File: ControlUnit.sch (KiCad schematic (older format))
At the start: 30 parts, among them U601 74HCT74N, U602 74HCT08N, U603 74LS153, U604 74HCT74N, U605 74HCT244N, U606 74HCT273N, U607 74HCT273N, U608 74LS161AN, U609 74HCT244N, U610 AT28C64B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

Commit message: Libraries re-imported.  Using rescue symbols still.  Adjusted multi-byte registers to use low-byte first.. applied this convention to all multi-byte registers for consistency.
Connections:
- net ~I[10:8]->BUS is gone; now on net ~I[7:5]->RS: U616.6
- net VCC: now also U604.4 (~S); no longer U604.1 (~R)
- net ~I[7:5]->RS: no longer U616.8
- net ~RST: now also U604.1 (~R); no longer U604.4 (~S)
- net ~sext(I[10:8])->BUS: now also U616.8
- net AREG_IN renamed ALU_AREG_IN
- net TR_HALT renamed TRG_HALT
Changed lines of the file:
@@
 IR_IN
 Text HLabel 14375 5050 2    50   Output ~ 0
-AREG_IN
+ALU_AREG_IN
 Text HLabel 11275 2175 2    50   Output ~ 0
 B2
@@
 $EndComp
 Text HLabel 14325 14475 2    50   Output ~ 0
-TR_HALT
+TRG_HALT
 $Comp
 L Breadboard_CPU-rescue:74LS04-74xx U616
@@
 	1    0    0    -1
 $EndComp
-Text HLabel 4375 8050 1    50   Input ~ 0
+Text HLabel 4375 8750 3    50   Input ~ 0
 ~RST
 Wire Wire Line
-	4375 8050 4375 8100
+	4375 8750 4375 8700
 $Comp
 L Breadboard_CPU-rescue:VCC-power #PWR?
 U 1 1 6109BDDC
-P 4375 8750
+P 4375 8050
 AR Path="/5EFC0623/6109BDDC" Ref="#PWR?"  Part="1"
 AR Path="/5F05F116/6109BDDC" Ref="#PWR0604"  Part="1"
-F 0 "#PWR0604" H 4375 8600 50  0001 C CNN
-F 1 "VCC" H 4393 8923 50  0000 C CNN
-F 2 "" H 4375 8750 50  0001 C CNN
-F 3 "" H 4375 8750 50  0001 C CNN
-	1    4375 8750
-	1    0    0    1
-$EndComp
-Wire Wire Line
-	4375 8700 4375 8750
+F 0 "#PWR0604" H 4375 7900 50  0001 C CNN
+F 1 "VCC" H 4393 8223 50  0000 C CNN
+F 2 "" H 4375 8050 50  0001 C CNN
+F 3 "" H 4375 8050 50  0001 C CNN
+	1    4375 8050
+	-1   0    0    -1
+$EndComp
+Wire Wire Line
+	4375 8100 4375 8050
 Wire Wire Line
 	4025 8300 4075 8300
@@
 Wire Wire Line
 	14375 5550 13475 5550
-Text Label 16250 11725 0    50   ~ 0
-~I[10:8]->BUS
+Text Label 16250 12225 0    50   ~ 0
+~sext(I[10:8])->BUS
 Text Label 16250 11225 0    50   ~ 0
 ~I[10:8]->RS
-Text Label 16250 12225 0    50   ~ 0
+Text Label 16250 11725 0    50   ~ 0
 ~I[7:5]->RS
 Text Label 16250 12725 0    50   ~ 0

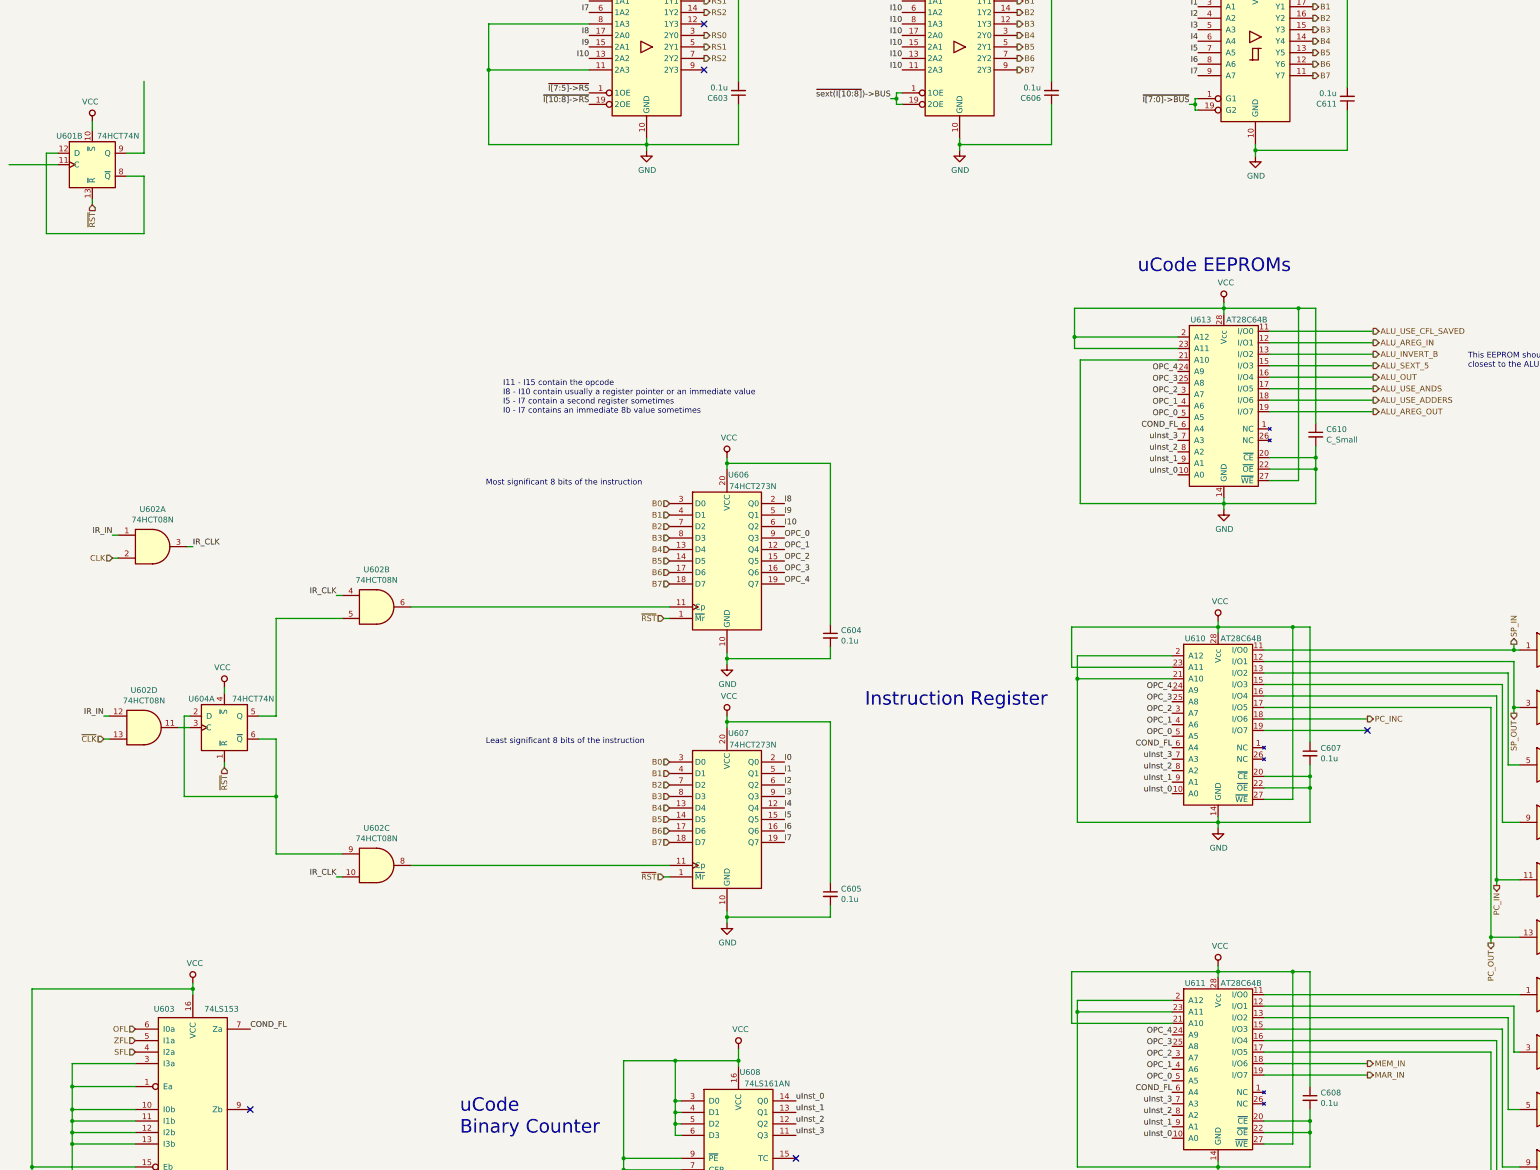
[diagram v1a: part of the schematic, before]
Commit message: Added REGS_ASSERT_RS0.  Added user referenceable CFL to solve issue of performing arithmetic on stack frame and global pointers.  TRAP routines will be created to perform ADD operations (leveraging JC/JNC) on SFP and GP.  uCode rev. 1 created in GDrive.
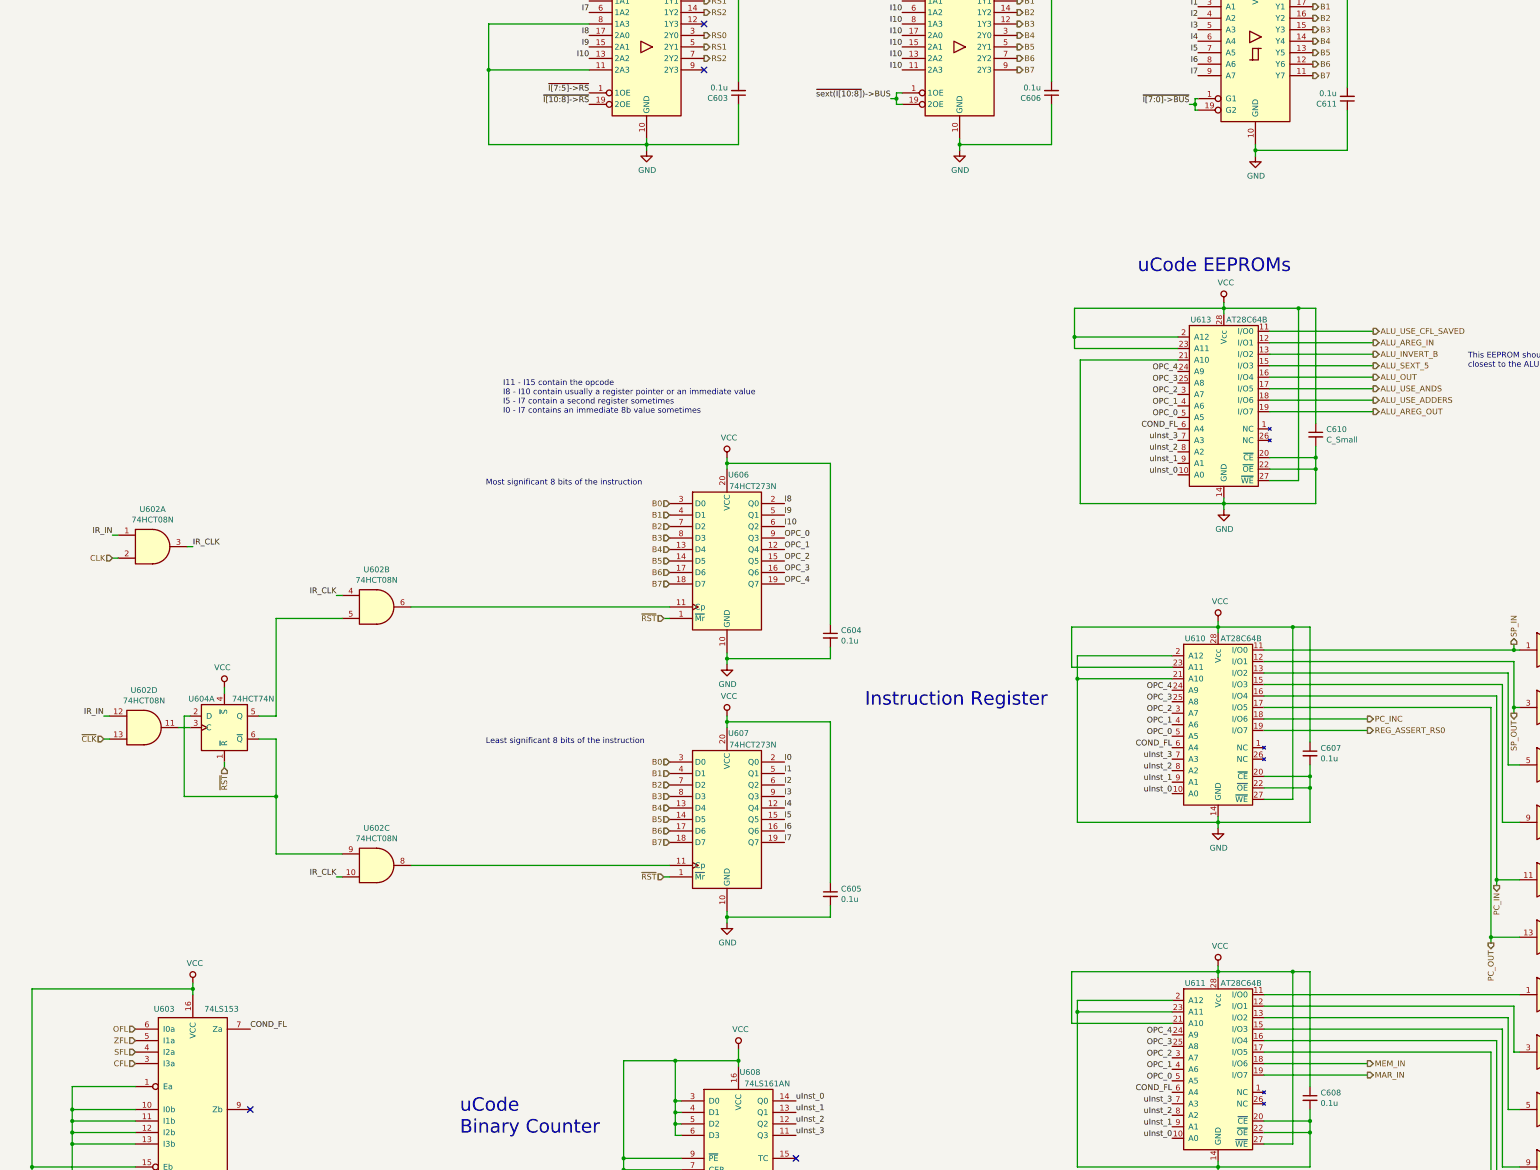
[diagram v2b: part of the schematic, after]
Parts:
- removed U601: 74HCT74N, symbol Breadboard_CPU-rescue:74LS74-74xx
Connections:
- net GND: no longer U603.3 (I3a)
- net REG_ASSERT_RS0: now reaches U610.19 (I/O7)
- new net CFL: U603.3 (I3a)
- no-connect marks 5 -> 4
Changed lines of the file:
@@
 ALU_INVERT_B
-$Comp
-L Breadboard_CPU-rescue:74LS74-74xx U601
-U 2 1 61164C73
-P 3225 3500
-AR Path="/5F05F116/61164C73" Ref="U601"  Part="2"
-AR Path="/5EFC0970/61164C73" Ref="U?"  Part="2"
-AR Path="/5EFC0623/61164C73" Ref="U?"  Part="2"
-F 0 "U601" H 3025 3750 50  0000 C CNN
-F 1 "74HCT74N" H 3450 3750 50  0000 C CNN
-F 2 "" H 3225 3500 50  0001 C CNN
-F 3 "74xx/74hc_hct74.pdf" H 3225 3500 50  0001 C CNN
-	2    3225 3500
-	1    0    0    -1
-$EndComp
-Text HLabel 3225 3850 3    50   Input ~ 0
-~RST
-Wire Wire Line
-	3225 3850 3225 3800
-$Comp
-L Breadboard_CPU-rescue:VCC-power #PWR?
-U 1 1 6119C7DB
-P 3225 3125
-AR Path="/5EFC0623/6119C7DB" Ref="#PWR?"  Part="1"
-AR Path="/5F05F116/6119C7DB" Ref="#PWR0601"  Part="1"
-F 0 "#PWR0601" H 3225 2975 50  0001 C CNN
-F 1 "VCC" H 3243 3298 50  0000 C CNN
-F 2 "" H 3225 3125 50  0001 C CNN
-F 3 "" H 3225 3125 50  0001 C CNN
-	1    3225 3125
-	-1   0    0    -1
-$EndComp
-Wire Wire Line
-	3225 3200 3225 3125
-Wire Wire Line
-	2825 3400 2925 3400
-Wire Wire Line
-	2825 4100 2825 3400
-Wire Wire Line
-	3675 4100 2825 4100
-Wire Wire Line
-	3675 3600 3675 4100
-Wire Wire Line
-	3525 3600 3675 3600
-Wire Wire Line
-	3525 3400 3675 3400
-Wire Wire Line
-	3675 3400 3675 2775
-Wire Wire Line
-	2925 3500 2500 3500
 $Comp
 L Breadboard_CPU-rescue:74LS08-74xx U?
@@
 Text HLabel 14375 4950 2    50   Output ~ 0
 ALU_USE_CFL_SAVED
-Wire Wire Line
-	3050 11525 3050 11325
-Wire Wire Line
-	3050 11325 3600 11325
-Connection ~ 3050 11525
 Text HLabel 3325 8500 0    50   Input ~ 0
 ~CLK
@@
 Text HLabel 15600 7675 1    50   Output ~ 0
 SP_IN
-NoConn ~ 14325 8425
 Text Label 3600 12525 2    50   ~ 0
 OPC_1
@@
 Text HLabel 14325 14275 2    50   Output ~ 0
 ALU_CFL_UPD
+Text HLabel 3600 11325 0    50   Input ~ 0
+CFL
+Text HLabel 14325 8425 2    50   Output ~ 0
+REG_ASSERT_RS0
 $EndSCHEMATC

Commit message: Pre-removal of H/L byte deciding hardware
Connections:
- net labels added: IRH_IN, IRL_IN, MARH_IN, MARL_IN, ~PCH_IN, ~PCH_OUT, ~PCL_IN, ~PCL_OUT
- net labels removed: MAR_IN
- wire segments 294 -> 292
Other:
- moved on the sheet: U602A, U602B, U602C, U602D, U604A
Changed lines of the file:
@@
 Text HLabel 14325 11325 2    50   Output ~ 0
 MEM_IN
-Text HLabel 14325 11425 2    50   Output ~ 0
-MAR_IN
+Text HLabel 18450 11575 2    50   Output ~ 0
+MARL_IN
 Wire Wire Line
 	13350 3425 13350 3375
@@
 Wire Wire Line
 	8300 11850 8300 11750
-Text Label 14325 13775 0    50   ~ 0
-IR_IN
+Text Label 18525 12425 0    50   ~ 0
+IRL_IN
 Text HLabel 14375 5050 2    50   Output ~ 0
 ALU_AREG_IN
@@
 L Breadboard_CPU-rescue:74LS08-74xx U?
 U 1 1 618B5634
-P 3750 6825
+P 5700 7350
 AR Path="/5EFC06D4/618B5634" Ref="U?"  Part="1"
 AR Path="/5F05F116/618B5634" Ref="U602"  Part="1"
-F 0 "U602" H 3750 7150 50  0000 C CNN
-F 1 "74HCT08N" H 3750 7059 50  0000 C CNN
-F 2 "" H 3750 6825 50  0001 C CNN
-F 3 "http://www.ti.com/lit/gpn/sn74LS08" H 3750 6825 50  0001 C CNN
-	1    3750 6825
-	1    0    0    -1
-$EndComp
-$Comp
-L Breadboard_CPU-rescue:74LS08-74xx U?
-U 2 1 618B563A
-P 5700 7350
-AR Path="/5EFC06D4/618B563A" Ref="U?"  Part="2"
-AR Path="/5F05F116/618B563A" Ref="U602"  Part="2"
 F 0 "U602" H 5700 7675 50  0000 C CNN
 F 1 "74HCT08N" H 5700 7584 50  0000 C CNN
 F 2 "" H 5700 7350 50  0001 C CNN
 F 3 "http://www.ti.com/lit/gpn/sn74LS08" H 5700 7350 50  0001 C CNN
-	2    5700 7350
+	1    5700 7350
+	1    0    0    -1
+$EndComp
+$Comp
+L Breadboard_CPU-rescue:74LS08-74xx U?
+U 2 1 618B563A
+P 5700 9600
+AR Path="/5EFC06D4/618B563A" Ref="U?"  Part="2"
+AR Path="/5F05F116/618B563A" Ref="U602"  Part="2"
+F 0 "U602" H 5700 9925 50  0000 C CNN
+F 1 "74HCT08N" H 5700 9834 50  0000 C CNN
+F 2 "" H 5700 9600 50  0001 C CNN
+F 3 "http://www.ti.com/lit/gpn/sn74LS08" H 5700 9600 50  0001 C CNN
+	2    5700 9600
 	1    0    0    -1
 $EndComp
@@
 Text HLabel 8250 6450 0    50   Input ~ 0
 B0
-Text HLabel 3400 6925 0    50   Input ~ 0
+Text HLabel 5350 7450 0    50   Input ~ 0
 CLK
 Wire Wire Line
-	3400 6925 3450 6925
-Wire Wire Line
-	3400 6725 3450 6725
-Text Label 3400 6725 2    50   ~ 0
-IR_IN
-Text Label 4100 6825 0    50   ~ 0
-IR_CLK
+	5350 7450 5400 7450
+Wire Wire Line
+	5350 7250 5400 7250
+Text Label 5350 7250 2    50   ~ 0
+IRL_IN
 $Comp
 L Breadboard_CPU-rescue:74LS74-74xx U?
 U 1 1 6109BDD4
-P 4375 8400
+P -5750 6700
 AR Path="/5EFC0970/6109BDD4" Ref="U?"  Part="1"
 AR Path="/5EFC0623/6109BDD4" Ref="U?"  Part="1"
 AR Path="/5F05F116/6109BDD4" Ref="U604"  Part="1"
-F 0 "U604" H 4175 8650 50  0000 C CNN
-F 1 "74HCT74N" H 4625 8650 50  0000 C CNN
-F 2 "" H 4375 8400 50  0001 C CNN
-F 3 "74xx/74hc_hct74.pdf" H 4375 8400 50  0001 C CNN
-	1    4375 8400
-	1    0    0    -1
-$EndComp
-Text HLabel 4375 8750 3    50   Input ~ 0
+F 0 "U604" H -5950 6950 50  0000 C CNN
+F 1 "74HCT74N" H -5500 6950 50  0000 C CNN
+F 2 "" H -5750 6700 50  0001 C CNN
+F 3 "74xx/74hc_hct74.pdf" H -5750 6700 50  0001 C CNN
+	1    -5750 6700
+	1    0    0    -1
+$EndComp
+Text HLabel -5750 7050 3    50   Input ~ 0
 ~RST
 Wire Wire Line
-	4375 8750 4375 8700
+	-5750 7050 -5750 7000
 $Comp
 L Breadboard_CPU-rescue:VCC-power #PWR?
 U 1 1 6109BDDC
-P 4375 8050
+P -5750 6350
 AR Path="/5EFC0623/6109BDDC" Ref="#PWR?"  Part="1"
 AR Path="/5F05F116/6109BDDC" Ref="#PWR0604"  Part="1"
-F 0 "#PWR0604" H 4375 7900 50  0001 C CNN
-F 1 "VCC" H 4393 8223 50  0000 C CNN
-F 2 "" H 4375 8050 50  0001 C CNN
-F 3 "" H 4375 8050 50  0001 C CNN
-	1    4375 8050
+F 0 "#PWR0604" H -5750 6200 50  0001 C CNN
+F 1 "VCC" H -5732 6523 50  0000 C CNN
+F 2 "" H -5750 6350 50  0001 C CNN
+F 3 "" H -5750 6350 50  0001 C CNN
+	1    -5750 6350
 	-1   0    0    -1
 $EndComp
 Wire Wire Line
-	4375 8100 4375 8050
-Wire Wire Line
-	4025 8300 4075 8300
-Wire Wire Line
-	4825 9000 4025 9000
-Wire Wire Line
-	4825 8500 4825 9000
-Wire Wire Line
-	4675 8500 4825 8500
-Wire Wire Line
-	4675 8300 4825 8300
+	-5750 6400 -5750 6350
+Wire Wire Line
+	-6100 6600 -6050 6600
+Wire Wire Line
+	-5300 7300 -6100 7300
+Wire Wire Line
+	-5300 6800 -5300 7300
+Wire Wire Line
+	-5450 6800 -5300 6800
+Wire Wire Line
+	-5450 6600 -5300 6600
 Text Label 10275 1975 2    50   ~ 0
 I8
@@
 L Breadboard_CPU-rescue:74LS08-74xx U?
 U 3 1 618B5640
-P 5700 9600
+P -4425 7900
 AR Path="/5EFC06D4/618B5640" Ref="U?"  Part="3"
 AR Path="/5F05F116/618B5640" Ref="U602"  Part="3"
-F 0 "U602" H 5700 9925 50  0000 C CNN
-F 1 "74HCT08N" H 5700 9834 50  0000 C CNN
-F 2 "" H 5700 9600 50  0001 C CNN
-F 3 "http://www.ti.com/lit/gpn/sn74LS08" H 5700 9600 50  0001 C CNN
-	3    5700 9600
+F 0 "U602" H -4425 8225 50  0000 C CNN
+F 1 "74HCT08N" H -4425 8134 50  0000 C CNN
+F 2 "" H -4425 7900 50  0001 C CNN
+F 3 "http://www.ti.com/lit/gpn/sn74LS08" H -4425 7900 50  0001 C CNN
+	3    -4425 7900
 	1    0    0    -1
 $EndComp
@@
 $EndComp
 Wire Wire Line
-	4100 6825 4050 6825
-Wire Wire Line
-	4025 9000 4025 8300
-Wire Wire Line
-	3975 8400 4075 8400
+	-6100 7300 -6100 6600
+Wire Wire Line
+	-6150 6700 -6050 6700
 Wire Wire Line
 	6000 9600 8250 9600
 Wire Wire Line
-	4825 7450 5400 7450
-Wire Wire Line
-	4825 7450 4825 8300
-Wire Wire Line
-	4825 9000 4825 9500
-Wire Wire Line
-	4825 9500 5400 9500
-Connection ~ 4825 9000
-Text Label 5350 7250 2    50   ~ 0
+	-5300 5750 -4725 5750
+Wire Wire Line
+	-5300 5750 -5300 6600
+Wire Wire Line
+	-5300 7300 -5300 7800
+Wire Wire Line
+	-5300 7800 -4725 7800
+Connection ~ -5300 7300
+Text Label -4775 5550 2    50   ~ 0
 IR_CLK
 Wire Wire Line
-	5350 7250 5400 7250
-Text Label 5350 9700 2    50   ~ 0
+	-4775 5550 -4725 5550
+Text Label -4775 8000 2    50   ~ 0
 IR_CLK
 Wire Wire Line
-	5350 9700 5400 9700
+	-4775 8000 -4725 8000
 Wire Wire Line
 	11800 15275 13025 15275
@@
 Wire Wire Line
 	11775 4750 13075 4750
-Text HLabel 16250 10225 2    50   Output ~ 0
+Text HLabel 17700 10175 2    50   Output ~ 0
 ~PC_OUT
-Text HLabel 16250 9725 2    50   Output ~ 0
+Text HLabel 17700 9675 2    50   Output ~ 0
 ~PC_IN
 Text HLabel 16250 13225 2    50   Output ~ 0
@@
 L Breadboard_CPU-rescue:74LS08-74xx U?
 U 4 1 618B5646
-P 3675 8400
+P -6450 6700
 AR Path="/5EFC06D4/618B5646" Ref="U?"  Part="4"
 AR Path="/5F05F116/618B5646" Ref="U602"  Part="4"
-F 0 "U602" H 3675 8725 50  0000 C CNN
-F 1 "74HCT08N" H 3675 8634 50  0000 C CNN
-F 2 "" H 3675 8400 50  0001 C CNN
-F 3 "http://www.ti.com/lit/gpn/sn74LS08" H 3675 8400 50  0001 C CNN
-	4    3675 8400
+F 0 "U602" H -6450 7025 50  0000 C CNN
+F 1 "74HCT08N" H -6450 6934 50  0000 C CNN
+F 2 "" H -6450 6700 50  0001 C CNN
+F 3 "http://www.ti.com/lit/gpn/sn74LS08" H -6450 6700 50  0001 C CNN
+	4    -6450 6700
 	1    0    0    -1
 $EndComp
 Text HLabel 14375 4950 2    50   Output ~ 0
 ALU_USE_CFL_SAVED
-Text HLabel 3325 8500 0    50   Input ~ 0
+Text HLabel -6800 6800 0    50   Input ~ 0
 ~CLK
 Wire Wire Line
-	3325 8500 3375 8500
-Wire Wire Line
-	3325 8300 3375 8300
-Text Label 3325 8300 2    50   ~ 0
+	-6800 6800 -6750 6800
+Wire Wire Line
+	-6800 6600 -6750 6600
+Text Label -6800 6600 2    50   ~ 0
 IR_IN
 Wire Wire Line
-	15450 9725 15450 9775
-Connection ~ 15450 9725
-Wire Wire Line
-	15400 10225 15400 10275
-Connection ~ 15400 10225
-Text HLabel 15450 9775 3    50   Output ~ 0
+	17525 9025 17525 9075
+Wire Wire Line
+	18525 8850 18525 8900
+Text HLabel 17525 9075 3    50   Output ~ 0
 PC_IN
-Text HLabel 15400 10275 3    50   Output ~ 0
+Text HLabel 18525 8900 3    50   Output ~ 0
 PC_OUT
 Text HLabel 14375 5350 2    50   Output ~ 0
@@
 Wire Wire Line
 	13425 7825 15600 7825
-Wire Wire Line
-	13425 7725 15600 7725
 Wire Wire Line
 	15600 8225 15650 8225
@@
 Wire Wire Line
 	16250 8225 16300 8225
-Text HLabel 16300 7725 2    50   Output ~ 0
+Text HLabel 17775 8900 2    50   Output ~ 0
 ~SP_IN
-Text HLabel 16300 8225 2    50   Output ~ 0
+Text HLabel 17775 9400 2    50   Output ~ 0
 ~SP_OUT
-Wire Wire Line
-	15600 8225 15600 8275
-Connection ~ 15600 8225
-Text HLabel 15600 8275 3    50   Output ~ 0
+Text HLabel 18250 8825 3    50   Output ~ 0
 SP_OUT
-Wire Wire Line
-	15600 7725 15600 7675
-Connection ~ 15600 7725
-Wire Wire Line
-	15600 7725 15650 7725
-Text HLabel 15600 7675 1    50   Output ~ 0
+Text HLabel 18250 8500 1    50   Output ~ 0
 SP_IN
 Text Label 3600 12525 2    50   ~ 0
@@
 Text HLabel 14325 8425 2    50   Output ~ 0
 REG_ASSERT_RS0
+Text HLabel 18450 11675 2    50   Output ~ 0
+MARH_IN
+Text HLabel 18800 11975 0    50   Output ~ 0
+~PCL_IN
+Text HLabel 18825 12100 0    50   Output ~ 0
+~PCH_IN
+Text HLabel 18900 12200 0    50   Output ~ 0
+~PCH_OUT
+Text HLabel 18850 12300 0    50   Output ~ 0
+~PCL_OUT
+Text HLabel 5350 9700 0    50   Input ~ 0
+CLK
+Wire Wire Line
+	5350 9700 5400 9700
+Wire Wire Line
+	5350 9500 5400 9500
+Text Label 5350 9500 2    50   ~ 0
+IRH_IN
+Text Label 18525 12525 0    50   ~ 0
+IRH_IN
+Wire Wire Line
+	13425 7725 15650 7725
 $EndSCHEMATC

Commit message: Testing memory module
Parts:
- removed U604: 74HCT74N, symbol Breadboard_CPU-rescue:74LS74-74xx
- added C?: C_Small, symbol Breadboard_CPU-rescue:C_Small-Device
- added U?: AT28C64B, symbol Memory:AT28C64B
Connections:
- net labels added: MEM_RD_HB, SPH_IN, SPH_OUT, SPL_IN, SPL_OUT
- net labels removed: IR_CLK, IR_IN, PC_IN, PC_OUT, SP_IN, SP_OUT, ~PC_IN, ~PC_OUT, ~SP_IN, ~SP_OUT
- wire segments 292 -> 305
- no-connect marks 4 -> 8
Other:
- moved on the sheet: C601, C602, C603, C604, C605, C606, C607, C608, C609, C610, C611, C612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
